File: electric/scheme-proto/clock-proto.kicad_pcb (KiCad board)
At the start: 2 copper layers, 134 parts, among them K1 servo, K2 1-wire, P1 batt, P10 led, P11 p2, P12 btn-4, P13 led, P14 led, P15 btn-5, P2 speaker, P3 dist, P4 btn-1, P5 btn-2, P6 btn-3, P7 led, P8 p1, P9 p3, Q1 bc857, Q10 bc847, Q11 bc847, Q12 bc857, Q13 bc857, Q14 bc847, Q15 bc847, Q16 bc847, Q17 bc857, Q18 bc857, Q2 bc847, Q3 bc857, Q4 bc847, Q5 irlml2244, Q6 bc847, Q7 bc857, Q8 bc847, Q9 bc857, U1 3310-LCD, U2 AD8607_2, U3 SD, U4 MINI-USB-B, U5 AD8607_2, U6 NCP3063, U7 NCP3063, U8 DS18S20

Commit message: Placing elements...
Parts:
- C8: value 4u7 -> 100n
- moved Q3 147.9 mm to (103.1, -36.3)
- moved Q1 147.6 mm to (103.1, -39.9)
- moved Q4 143.0 mm to (96.3, -35.6), turned to 90 degrees
- moved Q5 140.3 mm to (103.4, -32.0), turned to 90 degrees
- moved Q2 138.9 mm to (94.7, -41.1), turned to 90 degrees
- moved U2 137.2 mm to (74.9, 105.4)
- moved K1 133.8 mm to (106.9, -32.0), turned to 270 degrees
- moved U5 130.5 mm to (75.9, 93.6)
- moved P1 128.7 mm to (104.6, 39.6), turned to 270 degrees
- moved R13 119.3 mm to (74.4, 113.0), turned to 90 degrees
- moved Q14 118.1 mm to (70.9, 80.5)
- moved Q10 117.6 mm to (70.9, 91.1), turned to 180 degrees
- moved D2 117.4 mm to (98.0, 38.4), turned to 180 degrees
- moved C5 116.8 mm to (76.7, 111.0), turned to 90 degrees
- moved R6 116.1 mm to (75.9, 118.4), turned to 90 degrees
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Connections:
- C13 pad 1: /amp-vdd -> N-0000092
- C14 pad 1: /amp-vdd -> N-0000092
- P11 pad 26: /5v -> /from-discovery-5v
- Q13 pad 1: /amp-vdd -> N-0000092
- Q9 pad 3: /amp-vdd -> N-0000092
- R25 pad 1: /5v -> /from-discovery-5v
- R37 pad 2: /amp-vdd -> N-0000092
- U5 pad 5: /amp-vdd -> /filter-vdd
- U5 pad 8: /amp-vdd -> /filter-vdd

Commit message: Placing elements...
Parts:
- moved Q15 214.2 mm to (171.2, 112.5), turned to 90 degrees
- moved P7 212.2 mm to (173.5, 105.7)
- moved Q17 210.5 mm to (169.9, 109.0), turned to 270 degrees
- moved P6 206.8 mm to (174.9, 77.3)
- moved P4 203.7 mm to (174.9, 72.3)
- moved P15 199.9 mm to (146.6, 144.3), turned to 270 degrees
- moved P10 198.6 mm to (173.5, 103.1)
- moved P12 195.9 mm to (144.0, 144.3), turned to 270 degrees
- moved P13 194.7 mm to (173.5, 100.6)
- moved R47 190.8 mm to (173.0, 110.0), turned to 90 degrees
- moved R50 189.1 mm to (168.9, 105.7)
- moved R14 188.7 mm to (183.1, 99.1)
- moved R56 188.5 mm to (168.9, 100.6)
- moved R60 188.2 mm to (168.9, 98.0)
- moved P14 187.9 mm to (173.5, 98.0)
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
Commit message: Placing components and routing wires.
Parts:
- moved P2 85.4 mm to (79.9, 123.1), turned to 0 degrees
- moved R28 83.0 mm to (71.8, 116.7), turned to 0 degrees
- moved R29 79.9 mm to (71.8, 114.7), turned to 0 degrees
- moved R27 79.2 mm to (68.3, 111.1), turned to 0 degrees
- moved Q8 76.7 mm to (67.3, 108.6), turned to 0 degrees
- moved Q9 75.0 mm to (72.3, 111.9), turned to 90 degrees
- moved R26 73.4 mm to (67.3, 105.9), turned to 180 degrees
- moved C20 71.8 mm to (79.9, 115.4), turned to 180 degrees
- moved C21 71.8 mm to (79.9, 115.4), turned to 180 degrees
- moved C13 70.9 mm to (72.3, 109.1), turned to 180 degrees
- moved Q14 70.6 mm to (85.2, 117.2), turned to 180 degrees
- moved C14 68.5 mm to (72.3, 107.3), turned to 180 degrees
- moved Q13 63.9 mm to (85.2, 113.7), turned to 0 degrees
- moved C8 60.3 mm to (80.8, 109.2), turned to 180 degrees
- moved R37 58.3 mm to (84.2, 110.1), turned to 270 degrees
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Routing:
- net GND: track 0.00 -> 50.5 mm
- net VDD: track 0.00 -> 49.4 mm
- net /power: track 0.00 -> 26.2 mm
- net /from-adapter: track 0.00 -> 20.9 mm
- net N-00000125: track 0.00 -> 8.42 mm
- net N-0000025: track 0.00 -> 7.28 mm
- net /from-battery: track 0.00 -> 3.52 mm
- net /3v3: track 0.00 -> 3.14 mm
- net /from-discovery-5v: track 0.00 -> 2.94 mm
- net N-0000026: track 0.00 -> 1.98 mm

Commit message: Placing elements and routing...
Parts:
- moved Q7 75.7 mm to (159.9, 113.7), turned to 180 degrees
- moved R19 72.9 mm to (158.9, 117.3), turned to 90 degrees
- moved Q6 71.4 mm to (158.9, 120.7), turned to 180 degrees
- moved R18 71.0 mm to (160.0, 124.1), turned to 0 degrees
- moved C7 53.0 mm to (136.9, 115.7), turned to 90 degrees
- moved C14 26.1 mm to (52.3, 124.2)
- moved C8 26.1 mm to (60.8, 126.1)
- moved R24 26.1 mm to (61.2, 114.0)
- moved R35 26.1 mm to (66.3, 119.9)
- moved R39 26.1 mm to (66.3, 127.0)
- moved R28 26.1 mm to (51.8, 133.6)
- moved C9 26.1 mm to (58.7, 114.8)
- moved Q8 26.1 mm to (47.4, 125.5)
- moved U5 26.1 mm to (60.2, 121.0)
- moved C13 26.1 mm to (52.3, 126.0)
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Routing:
- net GND: track 50.5 -> 180.0 mm
- net VDD: track 49.4 -> 109.8 mm
- net N-00000103: track 0.00 -> 38.1 mm
- net /filter-vdd: track 0.00 -> 38.0 mm
- net N-00000101: track 0.00 -> 34.7 mm
- net N-0000095: track 0.00 -> 22.8 mm
- net /snd-amp-in: track 0.00 -> 18.9 mm
- net /5v-en: track 0.00 -> 16.0 mm
- net /5v: track 0.00 -> 13.2 mm
- net N-00000111: track 0.00 -> 8.74 mm
- net N-00000105: track 0.00 -> 8.29 mm
- net N-00000107: track 0.00 -> 7.71 mm
- net N-0000096: track 0.00 -> 5.22 mm
- net N-00000104: track 0.00 -> 4.57 mm
- net N-00000112: track 0.00 -> 4.06 mm
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
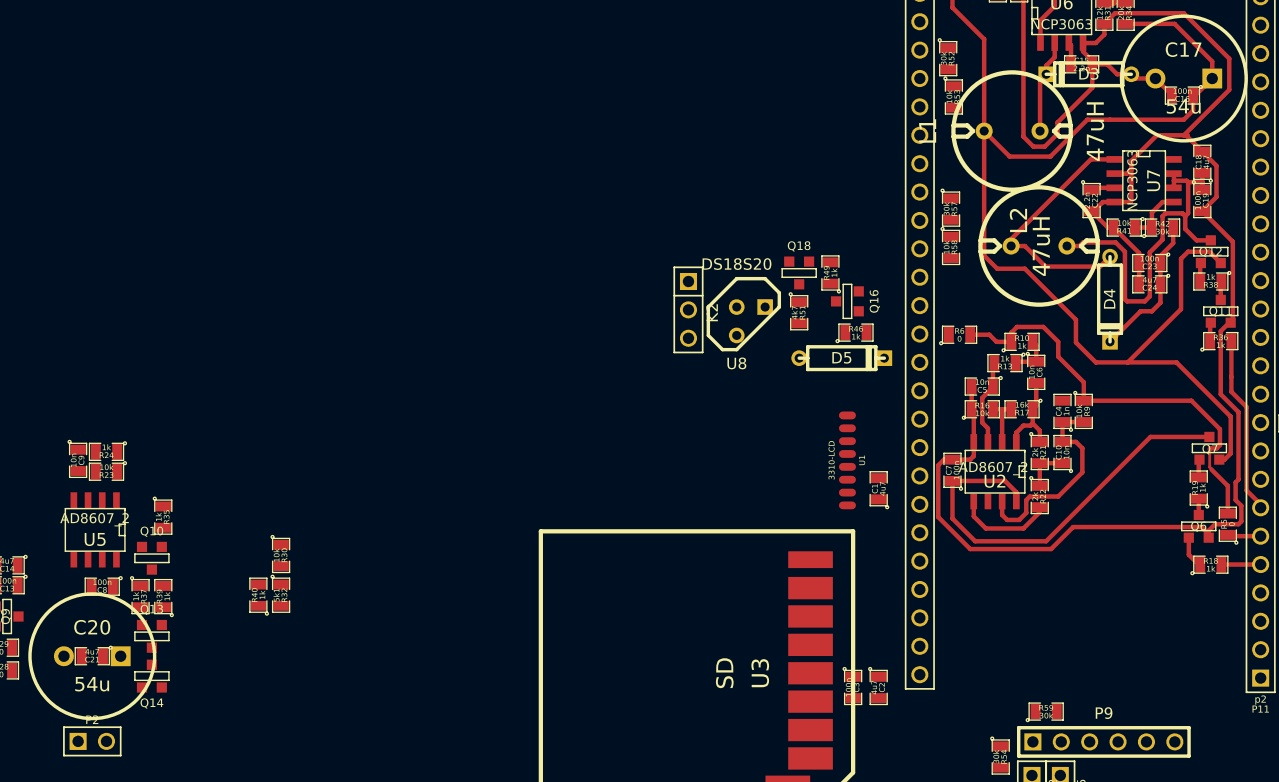
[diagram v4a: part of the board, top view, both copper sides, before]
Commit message: Placing components.
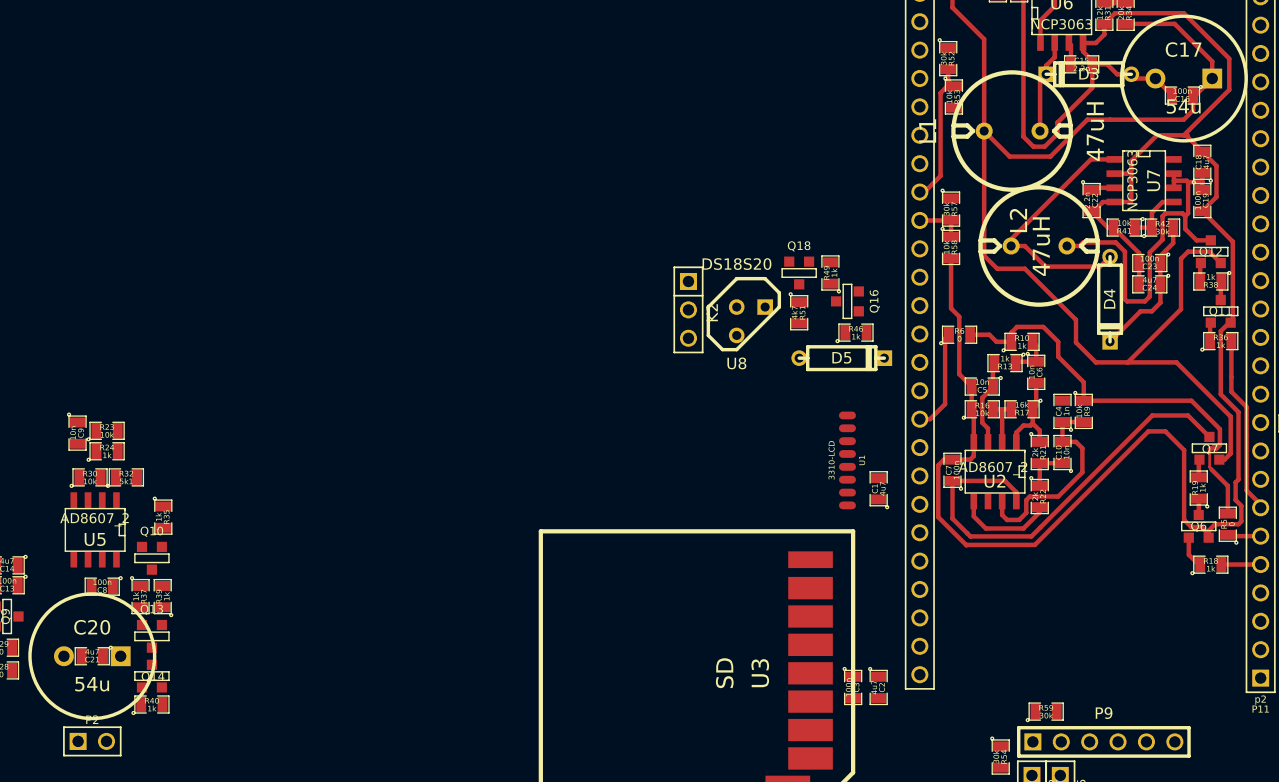
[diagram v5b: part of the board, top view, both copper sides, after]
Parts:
- moved R30 18.5 mm to (59.7, 116.3), turned to 0 degrees
- moved R32 17.4 mm to (63.0, 116.3), turned to 0 degrees
- moved R40 13.7 mm to (65.3, 136.7), turned to 0 degrees
- moved R23 3.66 mm to (61.3, 112.2), turned to 0 degrees
- moved C9 2.44 mm to (58.6, 112.4)
- moved R24 0.07 mm to (61.3, 114.0), turned to 0 degrees
- moved R39 0.05 mm to (66.2, 127.0)
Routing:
- net GND: track 180.0 -> 202.7 mm
- net /adapter-volt: track 0.00 -> 13.0 mm
- net /pa4: track 0.00 -> 9.17 mm
- net /battery-volt: track 0.00 -> 4.34 mm
- net /filter-vdd: track 38.0 -> 39.3 mm

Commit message: Routing...
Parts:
- moved R26 114.0 mm to (161.3, 125.3), turned to 0 degrees
- moved P2 109.0 mm to (168.9, 142.2), turned to 90 degrees
- moved Q8 108.1 mm to (154.8, 113.7)
- moved C21 104.7 mm to (164.2, 141.2), turned to 270 degrees
- moved C20 104.6 mm to (164.2, 141.2), turned to 270 degrees
- moved R27 104.4 mm to (152.0, 115.3), turned to 270 degrees
- moved C14 102.2 mm to (154.3, 117.5), turned to 90 degrees
- moved C13 101.5 mm to (153.7, 121.4), turned to 270 degrees
- moved Q9 99.8 mm to (151.6, 118.7), turned to 0 degrees
- moved Q13 95.4 mm to (160.5, 135.9)
- moved R39 95.3 mm to (161.4, 131.8)
- moved R40 93.9 mm to (159.1, 131.8), turned to 90 degrees
- moved R30 93.7 mm to (152.1, 131.7), turned to 180 degrees
- moved R37 92.4 mm to (156.7, 126.2), turned to 90 degrees
- moved U5 91.6 mm to (151.6, 126.7), turned to 0 degrees
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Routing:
- net GND: track 202.7 -> 419.2 mm, vias 0 -> 2
- net /power: track 26.4 -> 189.4 mm, vias 0 -> 2
- net VDD: track 109.8 -> 199.3 mm, vias 0 -> 2
- net /from-battery: track 3.52 -> 42.1 mm, vias 0 -> 1
- net /filter-vdd: track 39.3 -> 76.5 mm, vias 0 -> 2
- net /servo-vcc: track 0.00 -> 33.7 mm
- net N-0000023: track 0.00 -> 30.5 mm
- net /5v: track 13.2 -> 43.2 mm
- net /snd-amp-in: track 18.9 -> 47.1 mm, vias 0 -> 2
- net N-0000092: track 0.00 -> 27.2 mm
- net /from-adapter: track 20.9 -> 45.5 mm, vias 0 -> 1
- net N-00000107: track 7.71 -> 32.1 mm
- net N-0000083: track 0.00 -> 21.6 mm
- net /src: track 0.00 -> 20.3 mm, vias 0 -> 2
- net /btn-5: track 0.00 -> 19.3 mm
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
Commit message: Finished routing.
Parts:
- moved K2 27.6 mm to (129.4, 79.0), turned to 90 degrees
- moved U8 17.6 mm to (129.6, 88.4)
- moved R51 12.2 mm to (130.7, 92.0), turned to 180 degrees
- moved Q18 8.15 mm to (130.7, 94.9), turned to 180 degrees
- moved D5 7.19 mm to (127.7, 98.5), turned to 270 degrees
- moved R49 4.73 mm to (130.7, 97.9), turned to 180 degrees
- moved C3 4.59 mm to (128.4, 130.6), turned to 90 degrees
- moved C2 4.57 mm to (130.5, 130.6), turned to 90 degrees
- moved Q16 3.20 mm to (130.7, 100.7), turned to 180 degrees
- moved R46 2.44 mm to (130.7, 103.5)
- moved U3 1.71 mm to (124.6, 132.2), turned to 90 degrees
- moved U1 0.41 mm to (127.9, 114.8)
- moved C1 0.15 mm to (130.3, 117.2)
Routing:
- net GND: track 419.2 -> 606.5 mm
- net VDD: track 199.3 -> 289.5 mm
- net /pb15: track 0.00 -> 61.1 mm
- net /pb13: track 0.00 -> 38.4 mm
- net /1w-rx: track 0.00 -> 38.1 mm
- net /pb14: track 0.00 -> 37.4 mm
- net /pb12: track 0.00 -> 35.6 mm
- net /lcd-mode: track 0.00 -> 19.1 mm
- net N-0000015: track 0.00 -> 13.9 mm
- net /lcd-cs: track 0.00 -> 10.8 mm
- net /lcd-mosi: track 0.00 -> 10.1 mm
- net /1w-tx: track 0.00 -> 9.12 mm
- net /lcd-rst: track 0.00 -> 8.97 mm
- net /lcd-clk: track 0.00 -> 6.78 mm
- net N-00000129: track 0.00 -> 2.58 mm
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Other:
- board outline added: 63 x 88.5 mm

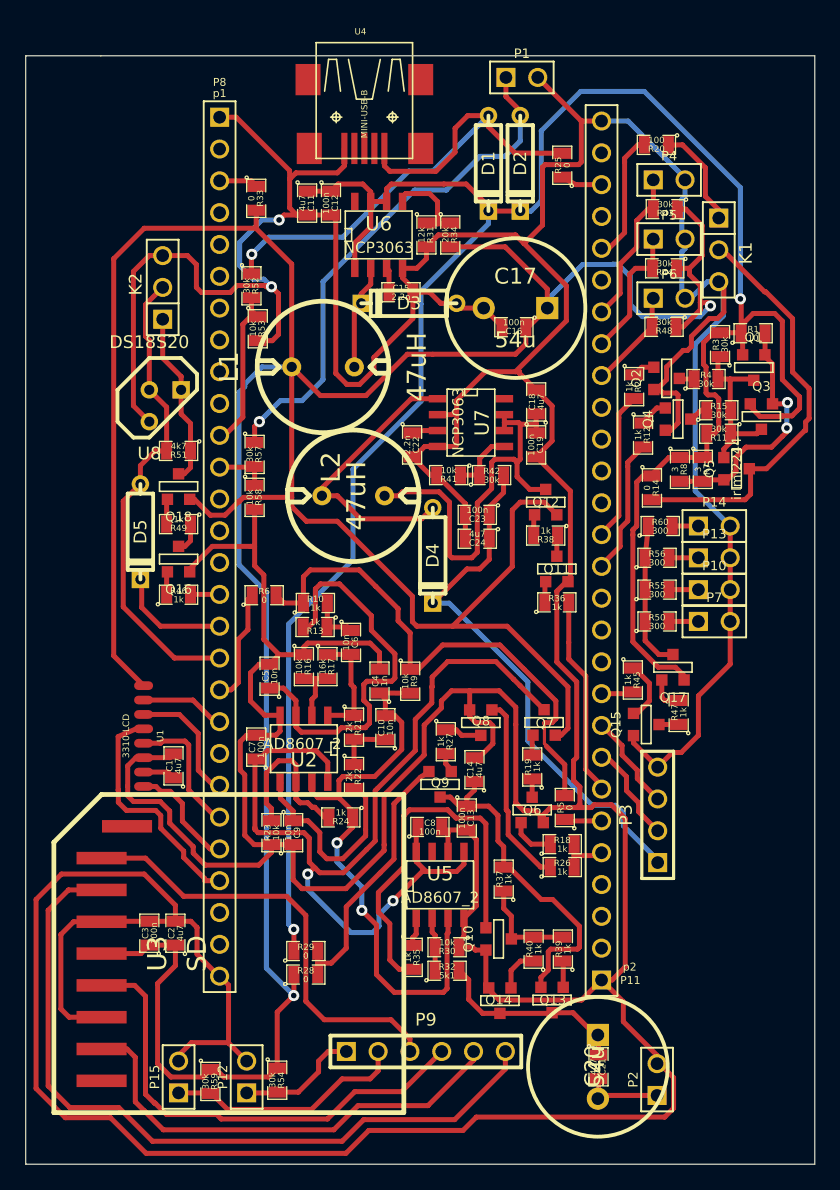
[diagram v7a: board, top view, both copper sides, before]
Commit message: Components list without unnecessary ones.
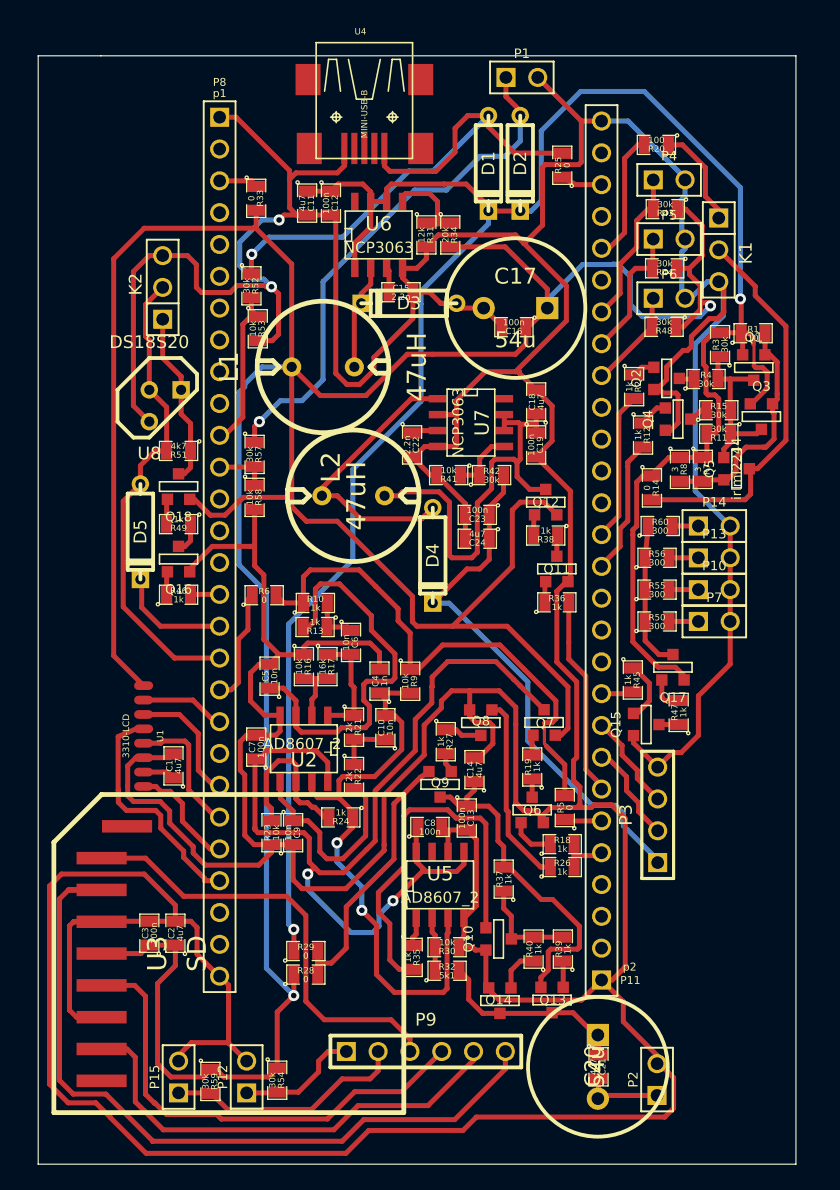
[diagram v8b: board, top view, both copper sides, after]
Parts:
- D5: value DIODESCH -> 1N5819
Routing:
- net /power: track 189.4 -> 180.9 mm
- net /servo-vcc: track 33.7 -> 31.4 mm
- net /src: track 20.3 -> 18.9 mm, vias 2 -> 0
- net /pb15: track 61.1 -> 62.2 mm
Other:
- board size 63 x 88.5 mm -> 60.5 x 88.5 mm
